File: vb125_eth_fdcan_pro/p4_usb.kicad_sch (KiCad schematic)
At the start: 0 parts

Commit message: AOZ schematic. 3V3 DC-DC. Partly bus power.
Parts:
- added C1 (x5): 10nF, symbol Device:C
- added D2: SMF22A, Diode_SMD:D_SMF, symbol Diode:SMF22A
- added D3: MM5Z10VT1G, Diode_SMD:D_SOD-523, symbol Diode:MM5Zxx
- added J3: USB_C_Receptacle_USB2.0, Connector_USB:USB_C_Receptacle_GCT_USB4105-xx-A_16P_TopMnt_Horizontal, symbol Connector:USB_C_Receptacle_USB2.0
- added Q1, Q2: BSS138, Package_TO_SOT_SMD:SOT-23, symbol Transistor_FET:BSS138
- added R18: 10k, symbol Device:R_Small
- added R19 (x3): 5K1, Resistor_SMD:R_0402_1005Metric, symbol Device:R
- added R19, R20, R21: ?R, Resistor_SMD:R_0402_1005Metric, symbol Device:R
- added U3: USB3315, vhrd_interface_usb:QFN24_MICROCHIP, symbol vhrd_interface_usb:USB3315
- added X1: 24MHz, Oscillator:Oscillator_SMD_Abracon_ASE-4Pin_3.2x2.5mm, symbol Oscillator:ASE-xxxMHz
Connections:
- new net: Q1.3 (D), R19.2
- new net: R18.1, X1.1 (EN)
- new net: R19.1, X1.3 (OUT)
- new net: R19.2, R20.1, R21.1
- new net: R20.2, U3.23 (REFCLK)
- new net: Q2.3 (D), R19.2
- new net +3V3_DCDC: C1.1, R18.2, X1.4 (Vdd)
- new net +VIN_USB: C1.1, C1.1, C1.1, C1.1, D2.1 (A1), J3.A4 (VBUS), J3.A9 (VBUS), J3.B4 (VBUS), J3.B9 (VBUS), R19.1
- new net CC1: J3.A5 (CC1), R19.1
- new net CC2: J3.B5 (CC2), R19.1
- new net DM: J3.A7 (D-), J3.B7 (D-), U3.5 (DM)
- new net DP: J3.A6 (D+), J3.B6 (D+), U3.6 (DP)
- new net GND: C1.2, C1.2, C1.2, C1.2, C1.2, D2.2 (A2), D3.2 (A), J3.A1 (GND), J3.A12 (GND), J3.B1 (GND), J3.B12 (GND), Q1.2 (S), Q2.2 (S), U3.25 (GND), X1.2 (GND)
- new net H7_CLK: R21.2
- new net ULPI_CK: U3.12 (CLKOUT)
- new net ULPI_D0: U3.16 (DATA0)
- new net ULPI_D1: U3.15 (DATA1)
- new net ULPI_D2: U3.14 (DATA2)
- new net ULPI_D3: U3.13 (DATA3)
- new net ULPI_D4: U3.11 (DATA4)
- new net ULPI_D5: U3.10 (DATA5)
- new net ULPI_D6: U3.9 (DATA6)
- new net ULPI_D7: U3.8 (DATA7)
- new net ULPI_DIR: U3.19 (DIR)
- new net ULPI_NXT: U3.18 (NXT)
- new net ULPI_STP: U3.20 (STP)
- new net ~{PD_MOD_PRES}: D3.1 (K), Q1.1 (G), Q2.1 (G), R19.2

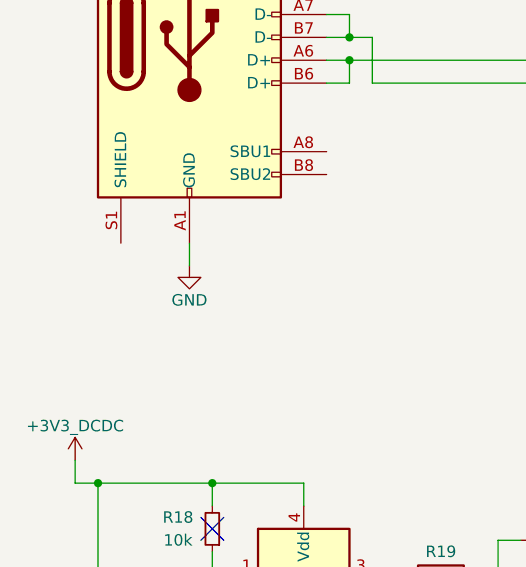
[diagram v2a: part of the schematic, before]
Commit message: CAN schematics. Assign IO on H7.
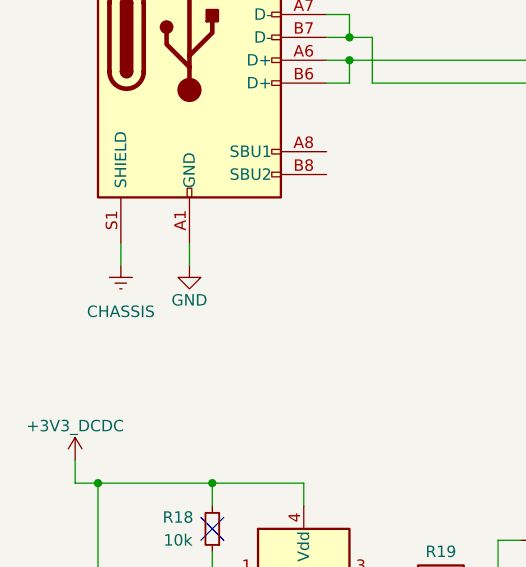
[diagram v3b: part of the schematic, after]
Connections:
- net CHASSIS: now reaches J3.S1 (SHIELD)
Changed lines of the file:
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@@
+    (stroke (width 0) (type default))
+  )
+  (wire (pts (xy 29.21 104.14) (xy 29.21 106.68))
     (stroke (width 0) (type default))
   )
@@
         )
       )
+    )
+  )
+  (symbol (lib_id "vhrd_power:CHASSIS") (at 29.21 106.68 0) (unit 1)
+    (in_bom yes) (on_board yes) (dnp no) (fields_autoplaced)
+    (property "Reference" "#PWR0153" (at 29.21 113.03 0)
+      (effects (font (size 1.27 1.27)) hide)
+    )
+    (property "Value" "CHASSIS" (at 29.21 111.76 0)
+      (effects (font (size 1.27 1.27)))
+    )
+    (property "Footprint" "" (at 29.21 106.68 0)
+      (effects (font (size 1.27 1.27)) hide)
+    )
+    (property "Datasheet" "~" (at 29.21 106.68 0)
+      (effects (font (size 1.27 1.27)) hide)
+    )
+    (pin "1")
+    (instances
+      (project "vb125_eth_fdcan_pro"
+        (path "/b473bccb-f14c-41d5-b473-137d3ef8ae1e/13d04be1-6d05-4847-9c03-a8fbeeb3fd19"
+          (reference "#PWR0153") (unit 1)
+        )
+      )

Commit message: Finish schematics.
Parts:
- removed D3: MM5Z10VT1G, Diode_SMD:D_SOD-523, symbol Diode:MM5Zxx
- removed Q1, Q2: BSS138, Package_TO_SOT_SMD:SOT-23, symbol Transistor_FET:BSS138
- removed R19: 5K1, Resistor_SMD:R_0402_1005Metric, symbol Device:R
- added C1: 4.7uF, Capacitor_SMD:C_0603_1608Metric, symbol Device:C
- added C2 (x2): 100nF, Capacitor_SMD:C_0402_1005Metric, symbol Device:C
- added C30 (x3): 1uF, Capacitor_SMD:C_0402_1005Metric, symbol Device:C
- added R19 (x2): 39R, Resistor_SMD:R_0402_1005Metric, symbol Device:R
- added R19, R9: 10K, Resistor_SMD:R_0402_1005Metric, symbol Device:R
- added U15: NCP563SQ18T1G, Package_TO_SOT_SMD:SC-82AB, symbol Regulator_Linear:NCP662SQ18
- C1: footprint (none) -> Capacitor_SMD:C_0402_1005Metric
- R18: footprint (none) -> Resistor_SMD:R_0402_1005Metric
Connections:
- net +3V3_DCDC: now also U3.17 (VDDIO), U3.3 (VBAT), C1.1, C2.1, C30.1, U15.2 (VIN), U15.4 (EN)
- net DM: now also R19.1
- net DP: now also R19.2
- net GND: now also R19.2, R19.2, C1.2, C2.2, C2.2, C30.2, C30.2, C30.2, R9.2, U15.1 (GND)
- net ULPI_VBUS: now reaches U3.2 (VBUS)
- net ULPI_VBUS: now also R19.2
- net +1V8_ULPI: now reaches U3.21 (VDD1.8)
- net +1V8_ULPI: now also C2.1, C30.1, U15.3 (VOUT)
- net ULPI_RST: now reaches U3.22 (RESETB)
- net ULPI_RBIAS: now reaches U3.24 (RBIAS)
- net ULPI_RBIAS: now also R9.1
- net ULPI_REGOUT_3V3: now reaches U3.4 (VDD3.3)
- net ULPI_REGOUT_3V3: now also C30.1
- new net +5V0_SYS: R19.1
- new net USBFS_DM: R19.2
- new net USBFS_DP: R19.1
- no-connect marks 0 -> 4
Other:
- note added: "1V8 LDO"
- note added: "ULPI REFCLK and H7 CLK"
- moved on the sheet: C1, D2, J3, R18, R19, R20, R21, U3, X1

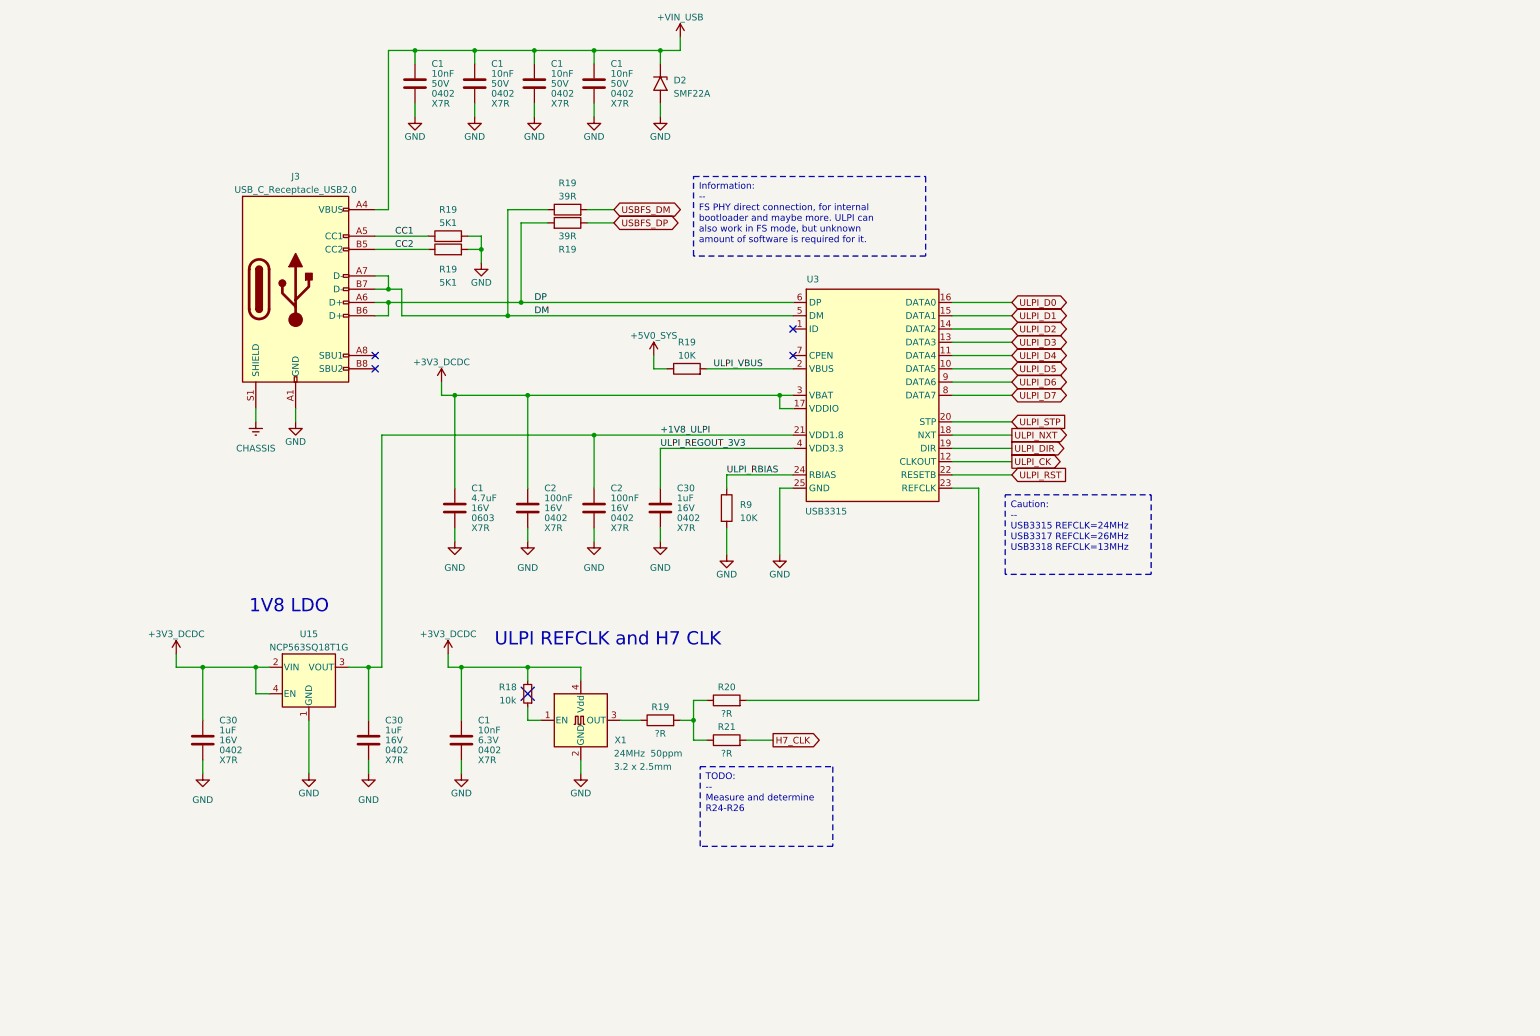
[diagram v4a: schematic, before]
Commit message: Add testpoints and set page templates.
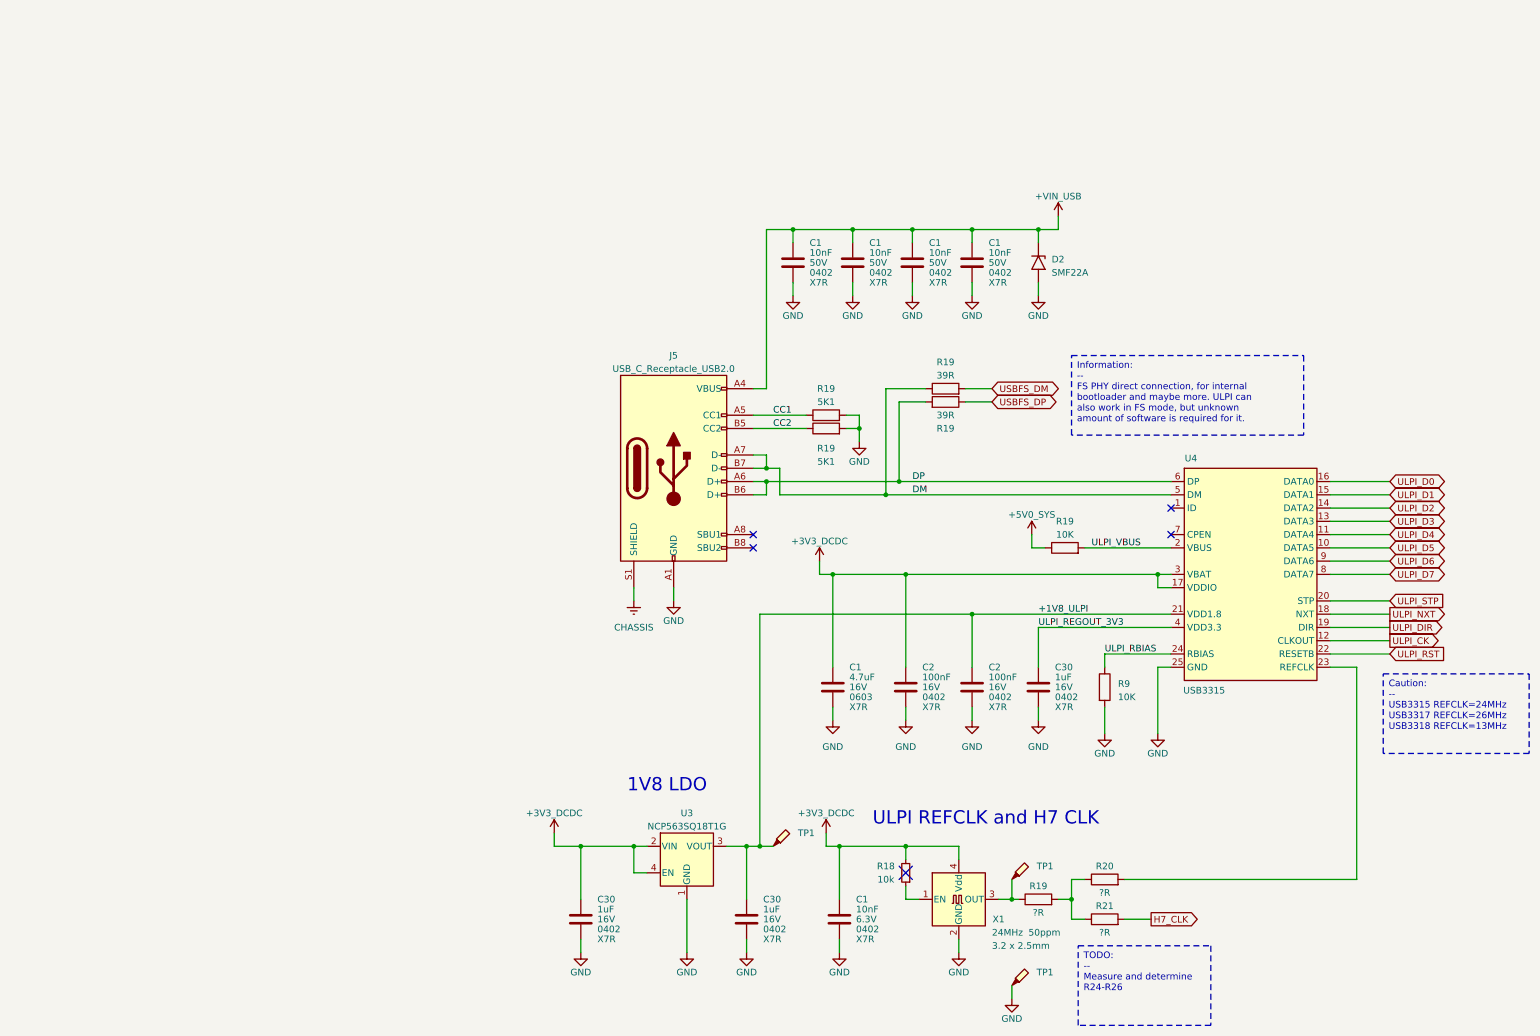
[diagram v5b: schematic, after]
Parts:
- added TP1 (x3): TestPoint_Probe, TestPoint:TestPoint_Pad_D1.5mm, symbol Connector:TestPoint_Probe
- renumbered J3 to J5, U15 to U3, U3 to U4
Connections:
- net +1V8_ULPI: now also TP1.1
- net GND: now also TP1.1
- net at R19.1, X1.3 (OUT): now also TP1.1
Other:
- company: (none) -> vhrd.tech AS
- title: (none) -> rt_bridge_pro
- moved on the sheet: C1, C2, C30, D2, J5, R18, R19, R20, R21, R9, U3, U4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

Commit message: Add sourcing information for resistors
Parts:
- R18: Mpn1 (none) -> RMCF0402FT10K0; Mpn2 (none) -> CR0402-FX-1002GLF
- R19: Mpn1 (none) -> RMCF0402FT5K10; Mpn2 (none) -> CR0402-FX-5101GLF; Mpn3 (none) -> RC0402FR-075K1L
- R19: Mpn1 (none) -> RMCF0402FT39R0; Mpn2 (none) -> CR0402-FX-39R0GLF; Mpn3 (none) -> RC0402FR-0739RL
- R19, R9: Mpn1 (none) -> RM04F1002CT; Mpn2 (none) -> RMCF0402FT10K0; Mpn3 (none) -> CR0402-FX-1002GLF
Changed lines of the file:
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@@
+      (effects (font (size 1.27 1.27)) hide)
+    )
+    (property "Mpn1" "RM04F1002CT" (at 227.33 149.86 0)
+      (effects (font (size 1.27 1.27)) hide)
+    )
+    (property "Mpn2" "RMCF0402FT10K0" (at 227.33 149.86 0)
+      (effects (font (size 1.27 1.27)) hide)
+    )
+    (property "Mpn3" "CR0402-FX-1002GLF" (at 227.33 149.86 0)
       (effects (font (size 1.27 1.27)) hide)
     )
@@
       (effects (font (size 1.27 1.27)) hide)
     )
+    (property "Mpn1" "RMCF0402FT5K10" (at 173.99 100.33 0)
+      (effects (font (size 1.27 1.27)) hide)
+    )
+    (property "Mpn2" "CR0402-FX-5101GLF" (at 173.99 100.33 0)
+      (effects (font (size 1.27 1.27)) hide)
+    )
+    (property "Mpn3" "RC0402FR-075K1L" (at 173.99 100.33 0)
+      (effects (font (size 1.27 1.27)) hide)
+    )
     (pin "1")
     (pin "2")
@@
     )
     (property "Datasheet" "~" (at 189.23 185.42 0)
+      (effects (font (size 1.27 1.27)) hide)
+    )
+    (property "Mpn1" "RMCF0402FT10K0" (at 189.23 185.42 0)
+      (effects (font (size 1.27 1.27)) hide)
+    )
+    (property "Mpn2" "CR0402-FX-1002GLF" (at 189.23 185.42 0)
       (effects (font (size 1.27 1.27)) hide)
     )
@@
       (effects (font (size 1.27 1.27)) hide)
     )
+    (property "Mpn1" "RMCF0402FT5K10" (at 173.99 97.79 0)
+      (effects (font (size 1.27 1.27)) hide)
+    )
+    (property "Mpn2" "CR0402-FX-5101GLF" (at 173.99 97.79 0)
+      (effects (font (size 1.27 1.27)) hide)
+    )
+    (property "Mpn3" "RC0402FR-075K1L" (at 173.99 97.79 0)
+      (effects (font (size 1.27 1.27)) hide)
+    )
     (pin "1")
     (pin "2")
@@
       (effects (font (size 1.27 1.27)) hide)
     )
+    (property "Mpn1" "RMCF0402FT39R0" (at 196.85 92.71 0)
+      (effects (font (size 1.27 1.27)) hide)
+    )
+    (property "Mpn2" "CR0402-FX-39R0GLF" (at 196.85 92.71 0)
+      (effects (font (size 1.27 1.27)) hide)
+    )
+    (property "Mpn3" "RC0402FR-0739RL" (at 196.85 92.71 0)
+      (effects (font (size 1.27 1.27)) hide)
+    )
     (pin "1")
     (pin "2")
@@
     )
     (property "Datasheet" "~" (at 219.71 123.19 0)
+      (effects (font (size 1.27 1.27)) hide)
+    )
+    (property "Mpn1" "RM04F1002CT" (at 219.71 123.19 0)
+      (effects (font (size 1.27 1.27)) hide)
+    )
+    (property "Mpn2" "RMCF0402FT10K0" (at 219.71 123.19 0)
+      (effects (font (size 1.27 1.27)) hide)
+    )
+    (property "Mpn3" "CR0402-FX-1002GLF" (at 219.71 123.19 0)
       (effects (font (size 1.27 1.27)) hide)
     )
@@
       (effects (font (size 1.27 1.27)) hide)
     )
+    (property "Mpn1" "RMCF0402FT39R0" (at 196.85 95.25 0)
+      (effects (font (size 1.27 1.27)) hide)
+    )
+    (property "Mpn2" "CR0402-FX-39R0GLF" (at 196.85 95.25 0)
+      (effects (font (size 1.27 1.27)) hide)
+    )
+    (property "Mpn3" "RC0402FR-0739RL" (at 196.85 95.25 0)
+      (effects (font (size 1.27 1.27)) hide)
+    )
